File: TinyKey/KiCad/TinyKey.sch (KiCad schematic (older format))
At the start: 103 parts, among them SW0:0 ESC, SW0:1 Q, SW0:10 P, SW0:11 EQ, SW0:12 BACK_SP, SW0:2 W, SW0:3 E, SW0:4 R, SW0:5 T, SW0:6 Y, SW0:7 U, SW0:8 I, SW0:9 O, SW1:0 TAB, SW1:1 A, SW1:10 COL, SW1:11 ENTER, SW1:2 S, SW1:3 D, SW1:4 F, SW1:5 G, SW1:6 H, SW1:7 J, SW1:8 K, SW1:9 L, SW2:0 L_SHIFT, SW2:1 Z, SW2:10 UP, SW2:11 R_SHIFT, SW2:12 PG_UP, SW2:2 X, SW2:3 C, SW2:4 V, SW2:5 B, SW2:6 N, SW2:7 M, SW2:8 L_ANG, SW2:9 R_ANG, SW3:0 L_CTRL, SW3:1 WIN_MOD, SW3:10 DOWN, SW3:11 RIGHT, SW3:12 PG_DOWN, SW3:2 L_ALT, SW3:3 L_META, SW3:5 SPACE, SW3:8 FN_HYPER, SW3:9 LEFT, U1 TEENSY

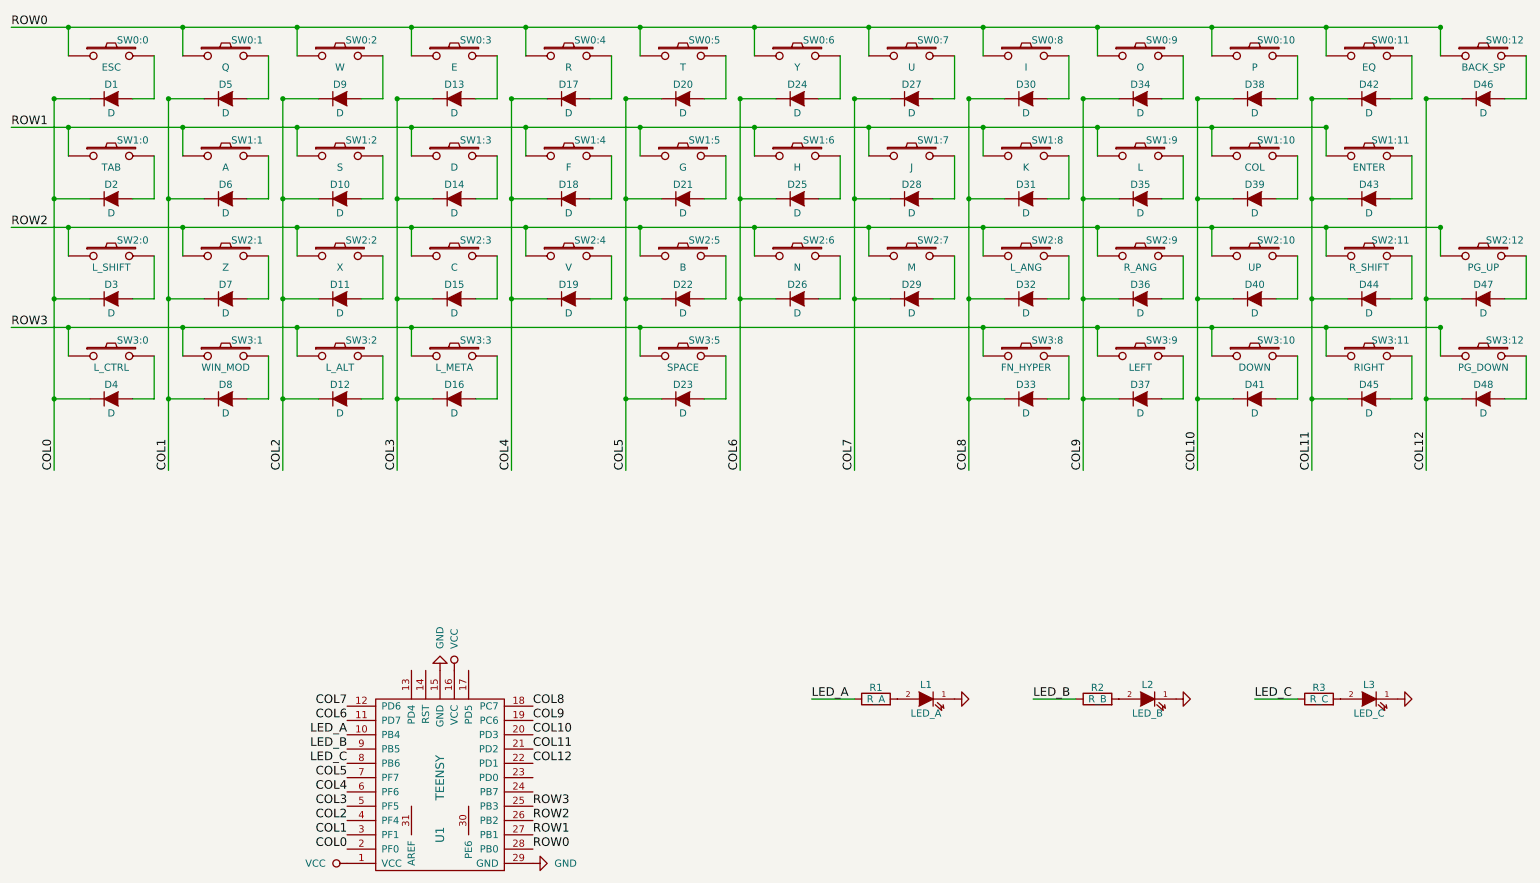
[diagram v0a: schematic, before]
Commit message: BlackRose V1 complete, Updated TinyKey to V2
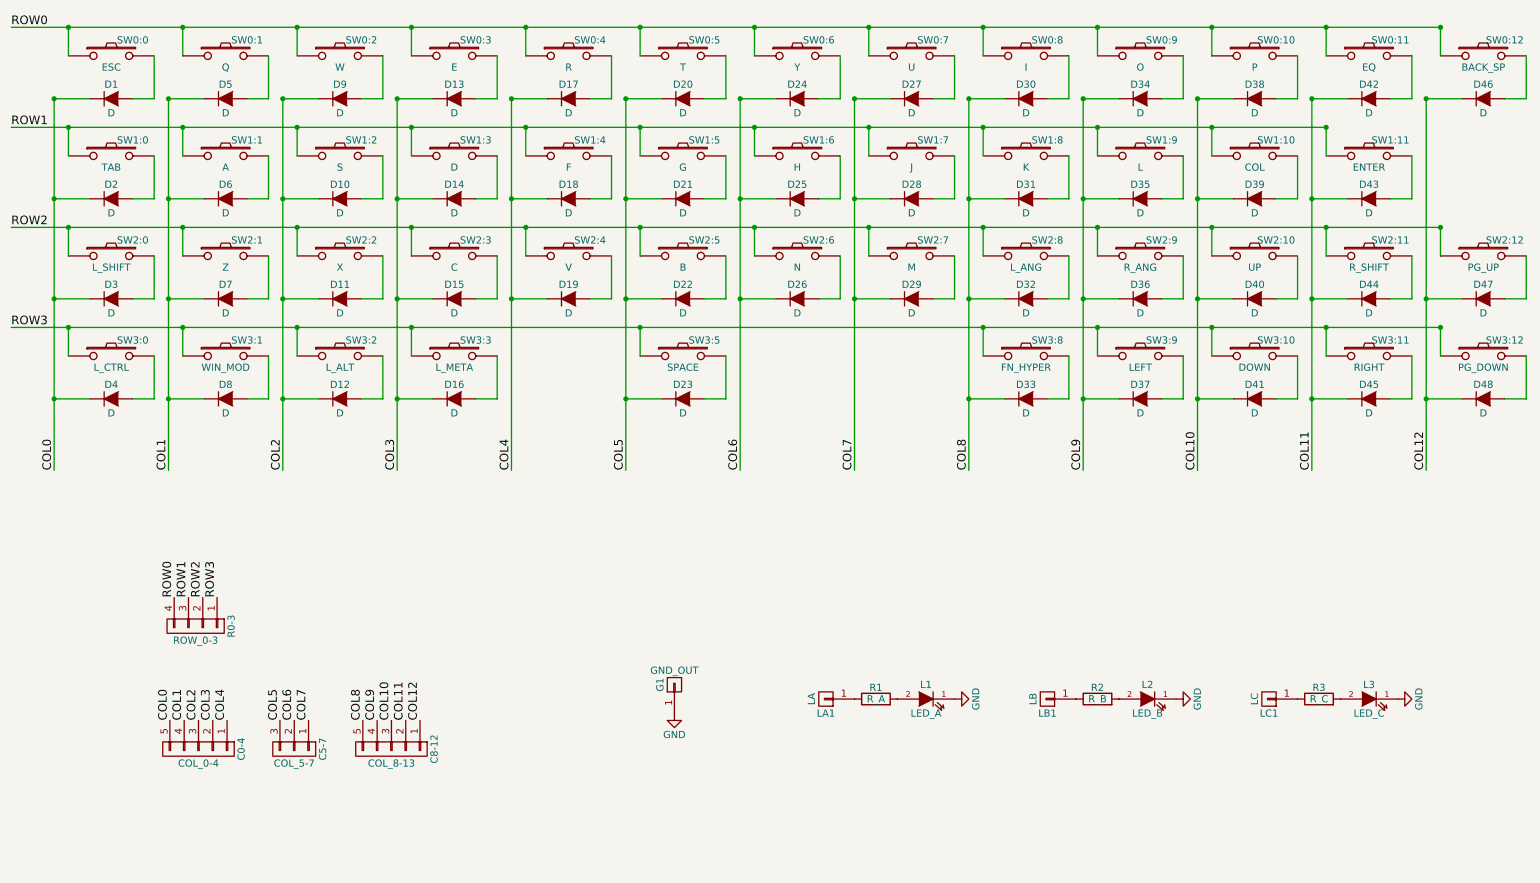
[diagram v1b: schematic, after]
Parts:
- removed U1: TEENSY, Cherry_MX:TEENSY_2.0, symbol TEENSY2.0
- added C0-4: COL_0-4, Pin_Headers:Pin_Header_Straight_1x05, symbol CONN_01X05
- added C5-7: COL_5-7, Pin_Headers:Pin_Header_Straight_1x03, symbol CONN_01X03
- added C8-12: COL_8-13, Pin_Headers:Pin_Header_Straight_1x05, symbol CONN_01X05
- added G1: GND_OUT, Pin_Headers:Pin_Header_Straight_1x01, symbol CONN_01X01
- added LA1: LA, Pin_Headers:Pin_Header_Straight_1x01, symbol CONN_01X01
- added LB1: LB, Pin_Headers:Pin_Header_Straight_1x01, symbol CONN_01X01
- added LC1: LC, Pin_Headers:Pin_Header_Straight_1x01, symbol CONN_01X01
- added R0-3: ROW_0-3, Pin_Headers:Pin_Header_Straight_1x04, symbol CONN_01X04
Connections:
- net COL0: now also C0-4.5 (P5)
- net COL1: now also C0-4.4 (P4)
- net COL10: now also C8-12.3 (P3)
- net COL11: now also C8-12.2 (P2)
- net COL12: now also C8-12.1 (P1)
- net COL2: now also C0-4.3 (P3)
- net COL3: now also C0-4.2 (P2)
- net COL4: now also C0-4.1 (P1)
- net COL5: now also C5-7.3 (P3)
- net COL6: now also C5-7.2 (P2)
- net COL7: now also C5-7.1 (P1)
- net COL8: now also C8-12.5 (P5)
- net COL9: now also C8-12.4 (P4)
- net GND: now also G1.1 (P1)
- net ROW0: now also R0-3.4 (P4)
- net ROW1: now also R0-3.3 (P3)
- net ROW2: now also R0-3.2 (P2)
- net ROW3: now also R0-3.1 (P1)
- net LED_A: no longer names the net of R1.1
- net LED_A: now also LA1.1 (P1)
- net LED_B: no longer names the net of R2.1
- net LED_B: now also LB1.1 (P1)
- net LED_C: no longer names the net of R3.1
- net LED_C: now also LC1.1 (P1)
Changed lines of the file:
@@
 Text Label 550  2900 0    60   ~ 0
 ROW3
-Text Label 850  3900 1    60   ~ 0
-COL0
-Text Label 1650 3900 1    60   ~ 0
-COL1
-Text Label 2450 3900 1    60   ~ 0
-COL2
-Text Label 3250 3900 1    60   ~ 0
-COL3
-Text Label 4050 3900 1    60   ~ 0
-COL4
-Text Label 4850 3900 1    60   ~ 0
-COL5
-Text Label 5650 3900 1    60   ~ 0
-COL6
-Text Label 6450 3900 1    60   ~ 0
-COL7
-Text Label 7250 3900 1    60   ~ 0
-COL8
 Text Label 8050 3900 1    60   ~ 0
 COL9
@@
 $EndComp
 $Comp
-L R R1
-U 1 1 57D29239
-P 6600 5500
-F 0 "R1" V 6680 5500 50  0000 C CNN
-F 1 "R_A" V 6600 5500 50  0000 C CNN
-F 2 "Cherry_MX:RESISTOR" V 6530 5500 50  0001 C CNN
-F 3 "" H 6600 5500 50  0000 C CNN
-	1    6600 5500
-	0    -1   -1   0
-$EndComp
-$Comp
-L GND #PWR01
-U 1 1 57D2AFFE
-P 7150 5500
-F 0 "#PWR01" H 7150 5250 50  0001 C CNN
-F 1 "GND" H 7150 5350 50  0001 C CNN
-F 2 "" H 7150 5500 50  0000 C CNN
-F 3 "" H 7150 5500 50  0000 C CNN
-	1    7150 5500
-	0    -1   -1   0
-$EndComp
-$Comp
 L LED L2
 U 1 1 57D2B9BB
@@
 $EndComp
 $Comp
-L GND #PWR02
-U 1 1 57D2B9C7
-P 8700 5500
-F 0 "#PWR02" H 8700 5250 50  0001 C CNN
-F 1 "GND" H 8700 5350 50  0001 C CNN
-F 2 "" H 8700 5500 50  0000 C CNN
-F 3 "" H 8700 5500 50  0000 C CNN
-	1    8700 5500
-	0    -1   -1   0
-$EndComp
-$Comp
 L LED L3
 U 1 1 57D2BAB5
@@
 $EndComp
 $Comp
+L CONN_01X04 R0-3
+U 1 1 5833D66B
+P 1840 4990
+F 0 "R0-3" H 1840 5240 50  0000 C CNN
+F 1 "ROW_0-3" V 1940 4990 50  0000 C CNN
+F 2 "Pin_Headers:Pin_Header_Straight_1x04" H 1840 4990 50  0001 C CNN
+F 3 "" H 1840 4990 50  0000 C CNN
+	1    1840 4990
+	0    1    1    0
+$EndComp
+Text Label 7250 3900 1    60   ~ 0
+COL8
+Text Label 6450 3900 1    60   ~ 0
+COL7
+Text Label 5650 3900 1    60   ~ 0
+COL6
+Text Label 4850 3900 1    60   ~ 0
+COL5
+Text Label 4050 3900 1    60   ~ 0
+COL4
+Text Label 3250 3900 1    60   ~ 0
+COL3
+Text Label 2450 3900 1    60   ~ 0
+COL2
+Text Label 1650 3900 1    60   ~ 0
+COL1
+Text Label 850  3900 1    60   ~ 0
+COL0
+$Comp
+L CONN_01X05 C0-4
+U 1 1 5833F2DB
+P 1860 5850
+F 0 "C0-4" H 1860 6150 50  0000 C CNN
+F 1 "COL_0-4" V 1960 5850 50  0000 C CNN
+F 2 "Pin_Headers:Pin_Header_Straight_1x05" H 1860 5850 50  0001 C CNN
+F 3 "" H 1860 5850 50  0000 C CNN
+	1    1860 5850
+	0    1    1    0
+$EndComp
+$Comp
+L CONN_01X05 C8-12
+U 1 1 5833F45F
+P 3210 5850
+F 0 "C8-12" H 3210 6150 50  0000 C CNN
+F 1 "COL_8-13" V 3310 5850 50  0000 C CNN
+F 2 "Pin_Headers:Pin_Header_Straight_1x05" H 3210 5850 50  0001 C CNN
+F 3 "" H 3210 5850 50  0000 C CNN
+	1    3210 5850
+	0    1    1    0
+$EndComp
+$Comp
+L CONN_01X03 C5-7
+U 1 1 5833F5C7
+P 2530 5850
+F 0 "C5-7" H 2530 6050 50  0000 C CNN
+F 1 "COL_5-7" V 2630 5850 50  0000 C CNN
+F 2 "Pin_Headers:Pin_Header_Straight_1x03" H 2530 5850 50  0001 C CNN
+F 3 "" H 2530 5850 50  0000 C CNN
+	1    2530 5850
+	0    1    1    0
+$EndComp
+Text Label 1690 4790 1    60   ~ 0
+ROW0
+Text Label 1790 4790 1    60   ~ 0
+ROW1
+Text Label 1890 4790 1    60   ~ 0
+ROW2
+Text Label 1990 4790 1    60   ~ 0
+ROW3
+Text Label 1660 5650 1    60   ~ 0
+COL0
+Text Label 1760 5650 1    60   ~ 0
+COL1
+Text Label 1860 5650 1    60   ~ 0
+COL2
+Text Label 1960 5650 1    60   ~ 0
+COL3
+Text Label 2060 5650 1    60   ~ 0
+COL4
+Text Label 2430 5650 1    60   ~ 0
+COL5
+Text Label 2530 5650 1    60   ~ 0
+COL6
+Text Label 2630 5650 1    60   ~ 0
+COL7
+Text Label 3010 5650 1    60   ~ 0
+COL8
+Text Label 3110 5650 1    60   ~ 0
+COL9
+Text Label 3210 5650 1    60   ~ 0
+COL10
+Text Label 3310 5650 1    60   ~ 0
+COL11
+Text Label 3410 5650 1    60   ~ 0
+COL12
+$Comp
+L CONN_01X01 G1
+U 1 1 58342F51
+P 5190 5400
+F 0 "G1" H 5190 5500 50  0000 C CNN
+F 1 "GND_OUT" V 5290 5400 50  0000 C CNN
+F 2 "Pin_Headers:Pin_Header_Straight_1x01" H 5190 5400 50  0001 C CNN
+F 3 "" H 5190 5400 50  0000 C CNN
+	1    5190 5400
+	0    -1   -1   0
+$EndComp
+$Comp
+L CONN_01X01 LC1
+U 1 1 58344876
+P 9350 5500
+F 0 "LC1" H 9350 5600 50  0000 C CNN
+F 1 "LC" V 9450 5500 50  0000 C CNN
+F 2 "Pin_Headers:Pin_Header_Straight_1x01" H 9350 5500 50  0001 C CNN
+F 3 "" H 9350 5500 50  0000 C CNN
+	1    9350 5500
+	-1   0    0    1
+$EndComp
+$Comp
+L R R1
+U 1 1 57D29239
+P 6600 5500
+F 0 "R1" V 6680 5500 50  0000 C CNN
+F 1 "R_A" V 6600 5500 50  0000 C CNN
+F 2 "Cherry_MX:RESISTOR" V 6530 5500 50  0001 C CNN
+F 3 "" H 6600 5500 50  0000 C CNN
+	1    6600 5500
+	0    -1   -1   0
+$EndComp
+$Comp
+L CONN_01X01 LB1
+U 1 1 58345A6D
+P 7800 5500
+F 0 "LB1" H 7800 5600 50  0000 C CNN
+F 1 "LB" V 7900 5500 50  0000 C CNN
+F 2 "Pin_Headers:Pin_Header_Straight_1x01" H 7800 5500 50  0001 C CNN
+F 3 "" H 7800 5500 50  0000 C CNN
+	1    7800 5500
+	-1   0    0    1
+$EndComp
+$Comp
+L CONN_01X01 LA1
+U 1 1 58345C04
+P 6250 5500
+F 0 "LA1" H 6250 5600 50  0000 C CNN
+F 1 "LA" V 6350 5500 50  0000 C CNN
+F 2 "Pin_Headers:Pin_Header_Straight_1x01" H 6250 5500 50  0001 C CNN
+F 3 "" H 6250 5500 50  0000 C CNN
+	1    6250 5500
+	-1   0    0    1
+$EndComp
+$Comp
+L GND #PWR01
+U 1 1 5834752E
+P 7150 5500
+F 0 "#PWR01" H 7150 5250 50  0001 C CNN
+F 1 "GND" H 7150 5350 50  0000 C CNN
+F 2 "" H 7150 5500 50  0000 C CNN
+F 3 "" H 7150 5500 50  0000 C CNN
+	1    7150 5500
+	0    -1   -1   0
+$EndComp
+$Comp
+L GND #PWR02
+U 1 1 58347848
+P 8700 5500
+F 0 "#PWR02" H 8700 5250 50  0001 C CNN
+F 1 "GND" H 8700 5350 50  0000 C CNN
+F 2 "" H 8700 5500 50  0000 C CNN
+F 3 "" H 8700 5500 50  0000 C CNN
+	1    8700 5500
+	0    -1   -1   0
+$EndComp
+$Comp
 L GND #PWR03
-U 1 1 57D2BAC1
+U 1 1 58347D2D
 P 10250 5500
 F 0 "#PWR03" H 10250 5250 50  0001 C CNN
-F 1 "GND" H 10250 5350 50  0001 C CNN
+F 1 "GND" H 10250 5350 50  0000 C CNN
 F 2 "" H 10250 5500 50  0000 C CNN
 F 3 "" H 10250 5500 50  0000 C CNN
@@
 	0    -1   -1   0
 $EndComp
-Text Label 6150 5500 0    60   ~ 0
-LED_A
-Wire Wire Line
-	6450 5500 6150 5500
-Wire Wire Line
-	7700 5500 8000 5500
-Wire Wire Line
-	9550 5500 9250 5500
-Text Label 7700 5500 0    60   ~ 0
-LED_B
-Text Label 9250 5500 0    60   ~ 0
-LED_C
-$Comp
-L TEENSY2.0 U1
-U 1 1 57D35245
-P 4000 6700
-F 0 "U1" V 4450 6450 60  0000 C CNN
-F 1 "TEENSY" V 4450 6050 60  0000 C CNN
-F 2 "Cherry_MX:TEENSY_2.0" H 4000 6700 60  0001 C CNN
-F 3 "" H 4000 6700 60  0001 C CNN
-	1    4000 6700
-	-1   0    0    1
-$EndComp
 $Comp
 L GND #PWR04
-U 1 1 57D361F3
-P 3550 5300
-F 0 "#PWR04" H 3550 5050 50  0001 C CNN
-F 1 "GND" V 3550 5150 50  0000 R CNN
-F 2 "" H 3550 5300 50  0000 C CNN
-F 3 "" H 3550 5300 50  0000 C CNN
-	1    3550 5300
-	1    0    0    1
-$EndComp
-$Comp
-L GND #PWR05
-U 1 1 57D3633C
-P 4200 6650
-F 0 "#PWR05" H 4200 6400 50  0001 C CNN
-F 1 "GND" V 4200 6500 50  0000 R CNN
-F 2 "" H 4200 6650 50  0000 C CNN
-F 3 "" H 4200 6650 50  0000 C CNN
-	1    4200 6650
-	0    -1   -1   0
-$EndComp
-$Comp
-L VCC #PWR06
-U 1 1 57D36553
-P 3650 5300
-F 0 "#PWR06" H 3650 5150 50  0001 C CNN
-F 1 "VCC" V 3650 5450 50  0000 L CNN
-F 2 "" H 3650 5300 50  0000 C CNN
-F 3 "" H 3650 5300 50  0000 C CNN
-	1    3650 5300
-	1    0    0    -1
-$EndComp
-$Comp
-L VCC #PWR07
-U 1 1 57D37C43
-P 2900 6650
-F 0 "#PWR07" H 2900 6500 50  0001 C CNN
-F 1 "VCC" V 2900 6800 50  0000 L CNN
-F 2 "" H 2900 6650 50  0000 C CNN
-F 3 "" H 2900 6650 50  0000 C CNN
-	1    2900 6650
-	0    -1   -1   0
-$EndComp
-Text Label 4200 6550 0    60   ~ 0
-ROW0
-Text Label 4200 6450 0    60   ~ 0
-ROW1
-Text Label 4200 6350 0    60   ~ 0
-ROW2
-Text Label 4200 6250 0    60   ~ 0
-ROW3
-Text Label 2900 5750 2    60   ~ 0
-LED_A
-Text Label 2900 5850 2    60   ~ 0
-LED_B
-Text Label 2900 5950 2    60   ~ 0
-LED_C
-Text Label 2900 6550 2    60   ~ 0
-COL0
-Text Label 2900 6450 2    60   ~ 0
-COL1
-Text Label 2900 6350 2    60   ~ 0
-COL2
-Text Label 2900 6250 2    60   ~ 0
-COL3
-Text Label 2900 6150 2    60   ~ 0
-COL4
-Text Label 2900 6050 2    60   ~ 0
-COL5
-Text Label 2900 5650 2    60   ~ 0
-COL6
-Text Label 2900 5550 2    60   ~ 0
-COL7
-Text Label 4200 5550 0    60   ~ 0
-COL8
-Text Label 4200 5650 0    60   ~ 0
-COL9
-Text Label 4200 5750 0    60   ~ 0
-COL10
-Text Label 4200 5850 0    60   ~ 0
-COL11
-Text Label 4200 5950 0    60   ~ 0
-COL12
+U 1 1 583480B5
+P 5190 5600
+F 0 "#PWR04" H 5190 5350 50  0001 C CNN
+F 1 "GND" H 5190 5450 50  0000 C CNN
+F 2 "" H 5190 5600 50  0000 C CNN
+F 3 "" H 5190 5600 50  0000 C CNN
+	1    5190 5600
+	1    0    0    -1
+$EndComp
 $EndSCHEMATC
